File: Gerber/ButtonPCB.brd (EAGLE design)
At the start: 42 x 22 mm, 7 parts, among them SW1 SPST_TACT-EVQQ2, SW2 SPST_TACT-EVQQ2, SW3 SPST_TACT-EVQQ2

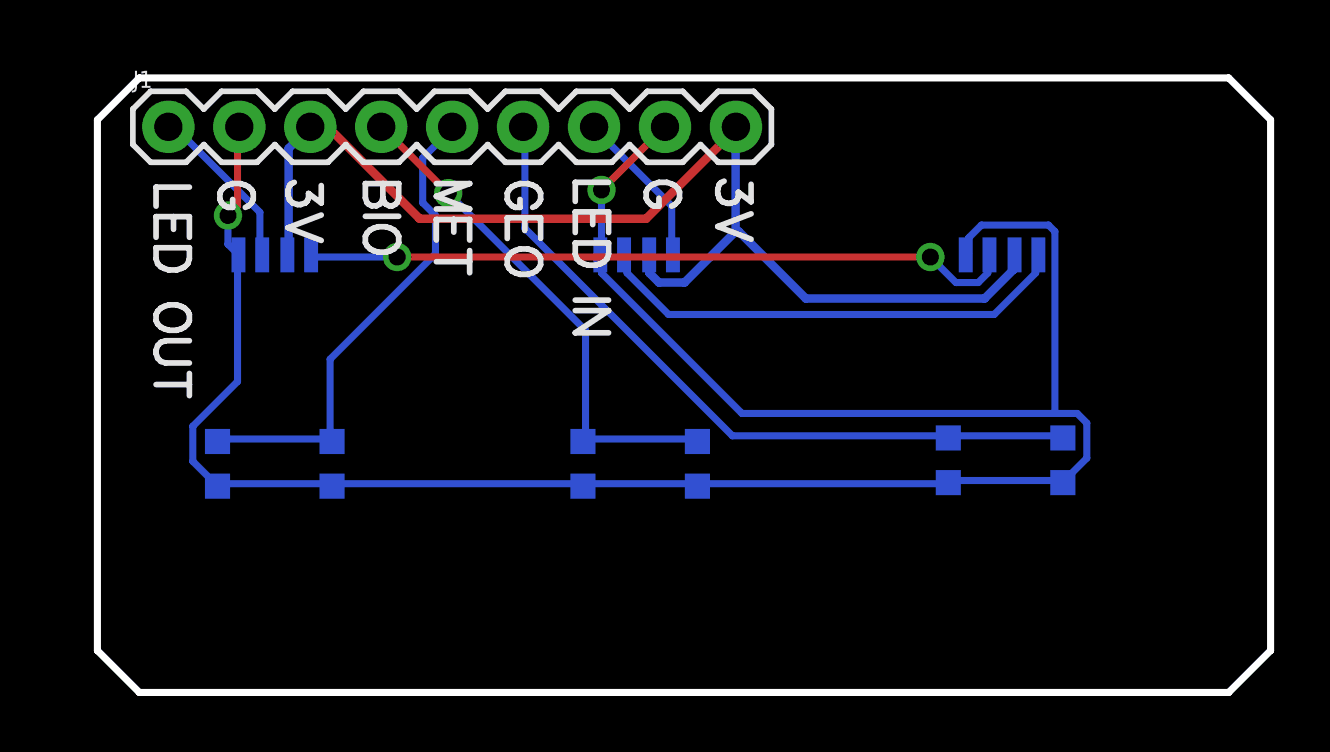
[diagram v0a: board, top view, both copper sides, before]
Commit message: Swapped to smd buttons that I like.
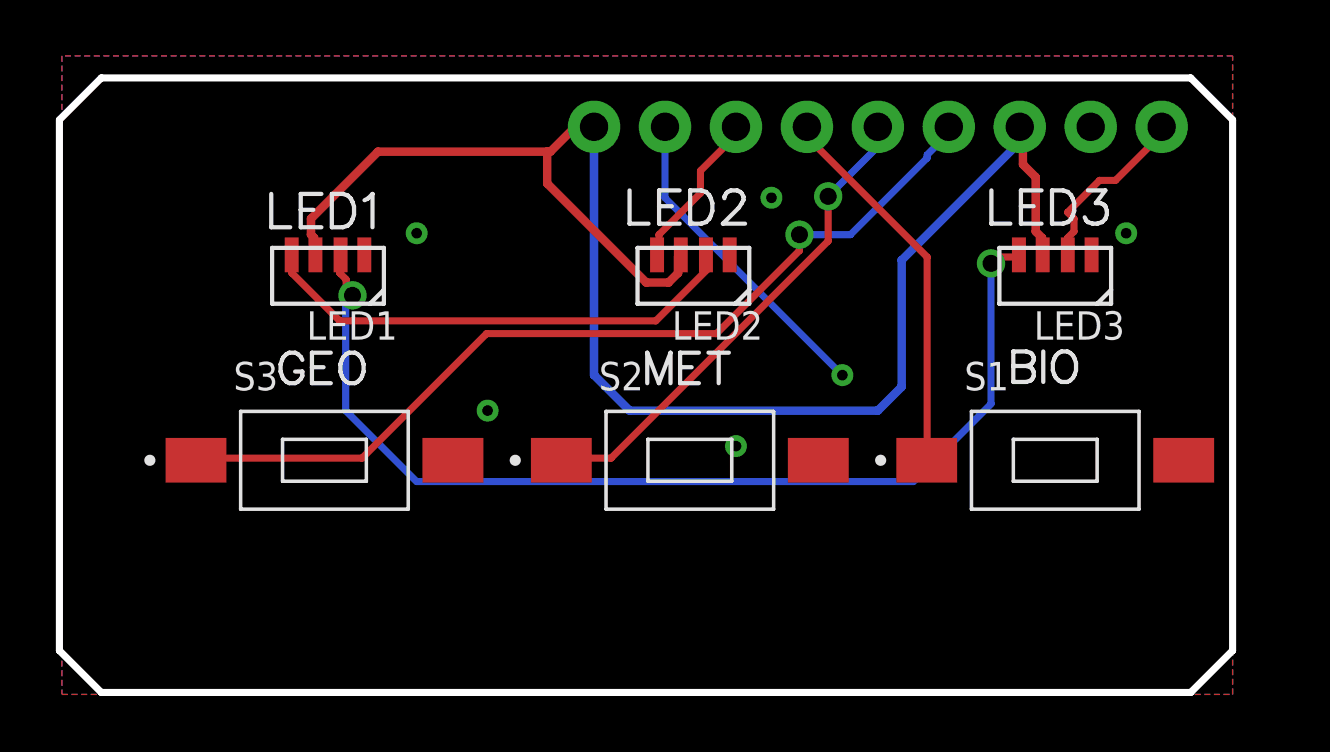
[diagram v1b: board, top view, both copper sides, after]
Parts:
- removed SW1, SW2, SW3: SPST_TACT-EVQQ2, microbuilder:BTN_KMR2_4.6X2.8
- added S1, S2, S3: 1437566-4, FSMSMTR-1437566-4:SW_1437566-4
- moved J1 35.6 mm to (39.4, 20.3), flipped to the bottom
- moved LED3 27.9 mm to (35.6, 15.0), flipped to the top
- moved LED1 24.1 mm to (9.53, 15.0), flipped to the top
- moved LED2 2.03 mm to (22.6, 15.0), flipped to the top
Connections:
- net BIO: now also S3.1; no longer SW3.A, SW3.A'
- net GEO: now also S1.1; no longer SW1.A, SW1.A'
- net GND: now also S1.2, S2.2, S3.2; no longer SW1.B, SW1.B', SW2.B, SW2.B', SW3.B, SW3.B'
- net MET: now also S2.1; no longer SW2.A, SW2.A'
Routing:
- net GND: track 83.8 -> 11.5 mm, vias 2 -> 6
- net V+: track 43.3 -> 57.9 mm
- net BIO: track 18.6 -> 32.5 mm
- net GEO: track 26.1 -> 13.7 mm
- net N$7: track 25.4 -> 37.3 mm
- net MET: track 17.7 -> 17.6 mm, vias 0 -> 1
- added copper zone on layer 1, net GND
- added copper zone on layer 16, net GND

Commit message: Added screw hole mounts to button pcb
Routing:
- net V+: track 57.9 -> 77.0 mm
- net N$6: track 17.5 -> 19.7 mm
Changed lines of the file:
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@@
 <setting verticaltext="up"/>
 </settings>
-<grid distance="0.05" unitdist="inch" unit="inch" style="lines" multiple="1" display="yes" altdistance="0.005" altunitdist="inch" altunit="inch"/>
+<grid distance="1" unitdist="mm" unit="mm" style="lines" multiple="1" display="yes" altdistance="0.1" altunitdist="mm" altunit="mm"/>
 <layers>
 <layer number="1" name="Top" color="4" fill="1" visible="yes" active="yes"/>
@@
 <layer number="44" name="Drills" color="7" fill="1" visible="no" active="yes"/>
 <layer number="45" name="Holes" color="7" fill="1" visible="yes" active="yes"/>
-<layer number="46" name="Milling" color="3" fill="1" visible="yes" active="yes"/>
+<layer number="46" name="Milling" color="3" fill="1" visible="no" active="yes"/>
 <layer number="47" name="Measures" color="7" fill="1" visible="no" active="yes"/>
 <layer number="48" name="Document" color="7" fill="1" visible="no" active="yes"/>
@@
 <wire x1="31.18045" y1="16.06071875" x2="31.12363125" y2="16.174359375" width="0.203" layer="22"/>
 <wire x1="31.12363125" y1="16.174359375" x2="31.12363125" y2="16.401640625" width="0.203" layer="22"/>
+<hole x="16.0655" y="14" drill="3.75"/>
+<hole x="29.083" y="14" drill="3.75"/>
 </plain>
 <attributes>
@@
 <wire x1="9.0297" y1="16.3449" x2="9.0297" y2="15.7734" width="0.3048" layer="1"/>
 <wire x1="8.9154" y1="16.4592" x2="9.0297" y2="16.3449" width="0.3048" layer="1"/>
-<wire x1="8.9154" y1="17.0307" x2="8.9154" y2="16.4592" width="0.3048" layer="1"/>
+<wire x1="8.9154" y1="17.0307" x2="8.9154" y2="16.8021" width="0.3048" layer="1"/>
+<wire x1="8.9154" y1="16.8021" x2="8.9154" y2="16.4592" width="0.3048" layer="1"/>
 <wire x1="11.3157" y1="19.431" x2="8.9154" y2="17.0307" width="0.3048" layer="1"/>
 <wire x1="17.4879" y1="19.431" x2="17.3736" y2="19.431" width="0.3048" layer="1"/>
@@
 <wire x1="17.3736" y1="19.431" x2="17.3736" y2="18.288" width="0.3048" layer="1"/>
 <wire x1="22.0599" y1="15.6591" x2="22.156" y2="15.736" width="0.3048" layer="1"/>
-<wire x1="34.29" y1="19.7739" x2="34.29" y2="20.32" width="0.3048" layer="16"/>
-<wire x1="30.0609" y1="15.5448" x2="34.29" y2="19.7739" width="0.3048" layer="16"/>
 <wire x1="19.0881" y1="20.2311" x2="19.05" y2="20.32" width="0.3048" layer="16"/>
-<wire x1="30.0609" y1="15.5448" x2="30.0609" y2="11.0109" width="0.3048" layer="16"/>
-<wire x1="30.0609" y1="11.0109" x2="29.21" y2="10.16" width="0.3048" layer="16"/>
-<wire x1="29.21" y1="10.16" x2="20.32" y2="10.16" width="0.3048" layer="16"/>
-<wire x1="20.32" y1="10.16" x2="19.05" y2="11.43" width="0.3048" layer="16"/>
-<wire x1="19.05" y1="11.43" x2="19.05" y2="20.32" width="0.3048" layer="16"/>
+<wire x1="35.0901" y1="10.0584" x2="35.0901" y2="15.6591" width="0.3048" layer="1"/>
+<wire x1="32.2326" y1="7.2009" x2="35.0901" y2="10.0584" width="0.3048" layer="1"/>
+<wire x1="3.5433" y1="7.2009" x2="32.2326" y2="7.2009" width="0.3048" layer="1"/>
+<wire x1="3.3147" y1="7.4295" x2="3.5433" y2="7.2009" width="0.3048" layer="1"/>
+<wire x1="3.3147" y1="12.2301" x2="3.3147" y2="7.4295" width="0.3048" layer="1"/>
+<wire x1="7.8867" y1="16.8021" x2="3.3147" y2="12.2301" width="0.3048" layer="1"/>
+<wire x1="8.9154" y1="16.8021" x2="7.8867" y2="16.8021" width="0.3048" layer="1"/>
+<wire x1="35.0901" y1="15.6591" x2="35.11" y2="15.736" width="0.3048" layer="1"/>
 </signal>
 <signal name="LED_IN">
@@
 <contactref element="LED1" pad="1"/>
 <contactref element="LED2" pad="3"/>
-<wire x1="8.2296" y1="15.0876" x2="8.2296" y2="15.6591" width="0.254" layer="1"/>
-<wire x1="9.9441" y1="13.3731" x2="8.2296" y2="15.0876" width="0.254" layer="1"/>
-<wire x1="21.2598" y1="13.3731" x2="9.9441" y2="13.3731" width="0.254" layer="1"/>
-<wire x1="23.0886" y1="15.2019" x2="21.2598" y2="13.3731" width="0.254" layer="1"/>
-<wire x1="23.0886" y1="15.6591" x2="23.0886" y2="15.2019" width="0.254" layer="1"/>
+<wire x1="8.2296" y1="15.2019" x2="8.2296" y2="15.6591" width="0.254" layer="1"/>
+<wire x1="10.0584" y1="13.3731" x2="8.2296" y2="15.2019" width="0.254" layer="1"/>
+<wire x1="11.0871" y1="13.3731" x2="10.0584" y2="13.3731" width="0.254" layer="1"/>
+<wire x1="14.7447" y1="17.0307" x2="11.0871" y2="13.3731" width="0.254" layer="1"/>
+<wire x1="17.9451" y1="17.0307" x2="14.7447" y2="17.0307" width="0.254" layer="1"/>
+<wire x1="20.8026" y1="14.1732" x2="17.9451" y2="17.0307" width="0.254" layer="1"/>
+<wire x1="21.9456" y1="14.1732" x2="20.8026" y2="14.1732" width="0.254" layer="1"/>
+<wire x1="22.9743" y1="15.2019" x2="21.9456" y2="14.1732" width="0.254" layer="1"/>
+<wire x1="22.9743" y1="15.6591" x2="22.9743" y2="15.2019" width="0.254" layer="1"/>
 <wire x1="8.2296" y1="15.6591" x2="8.225" y2="15.736" width="0.254" layer="1"/>
-<wire x1="23.0886" y1="15.6591" x2="23.056" y2="15.736" width="0.254" layer="1"/>
+<wire x1="22.9743" y1="15.6591" x2="23.056" y2="15.736" width="0.254" layer="1"/>
 </signal>
 <signal name="N$7">
@@
 <contactref element="J1" pad="4"/>
 <contactref element="S3" pad="1"/>
-<wire x1="10.7442" y1="8.4582" x2="4.8006" y2="8.4582" width="0.254" layer="1"/>
-<wire x1="15.2019" y1="12.9159" x2="10.7442" y2="8.4582" width="0.254" layer="1"/>
-<wire x1="23.4315" y1="12.9159" x2="15.2019" y2="12.9159" width="0.254" layer="1"/>
-<wire x1="26.4033" y1="15.8877" x2="23.4315" y2="12.9159" width="0.254" layer="1"/>
-<wire x1="26.4033" y1="16.4592" x2="26.4033" y2="15.8877" width="0.254" layer="1"/>
-<wire x1="28.2321" y1="16.4592" x2="26.4033" y2="16.4592" width="0.254" layer="16"/>
-<wire x1="30.9753" y1="19.2024" x2="28.2321" y2="16.4592" width="0.254" layer="16"/>
+<wire x1="11.6586" y1="8.4582" x2="4.8006" y2="8.4582" width="0.254" layer="1"/>
+<wire x1="14.1732" y1="10.9728" x2="11.6586" y2="8.4582" width="0.254" layer="1"/>
+<wire x1="20.574" y1="10.9728" x2="14.1732" y2="10.9728" width="0.254" layer="1"/>
+<wire x1="26.289" y1="16.6878" x2="20.574" y2="10.9728" width="0.254" layer="1"/>
+<wire x1="26.4033" y1="16.6878" x2="26.289" y2="16.6878" width="0.254" layer="16"/>
+<wire x1="26.6319" y1="16.4592" x2="26.4033" y2="16.6878" width="0.254" layer="16"/>
+<wire x1="27.2034" y1="16.4592" x2="26.6319" y2="16.4592" width="0.254" layer="16"/>
+<wire x1="27.6606" y1="16.9164" x2="27.2034" y2="16.4592" width="0.254" layer="16"/>
+<wire x1="27.7749" y1="16.9164" x2="27.6606" y2="16.9164" width="0.254" layer="16"/>
+<wire x1="28.575" y1="17.7165" x2="27.7749" y2="16.9164" width="0.254" layer="16"/>
+<wire x1="29.4894" y1="17.7165" x2="28.575" y2="17.7165" width="0.254" layer="16"/>
+<wire x1="30.9753" y1="19.2024" x2="29.4894" y2="17.7165" width="0.254" layer="16"/>
 <wire x1="30.9753" y1="19.3167" x2="30.9753" y2="19.2024" width="0.254" layer="16"/>
 <wire x1="31.6611" y1="20.0025" x2="30.9753" y2="19.3167" width="0.254" layer="16"/>
@@
 <wire x1="4.8006" y1="8.4582" x2="4.798" y2="8.382" width="0.254" layer="1"/>
 <wire x1="31.6611" y1="20.2311" x2="31.75" y2="20.32" width="0.254" layer="16"/>
-<via x="26.4033" y="16.4592" extent="1-16" drill="0.6096"/>
+<via x="26.289" y="16.6878" extent="1-16" drill="0.6096"/>
 </signal>
 </signals>

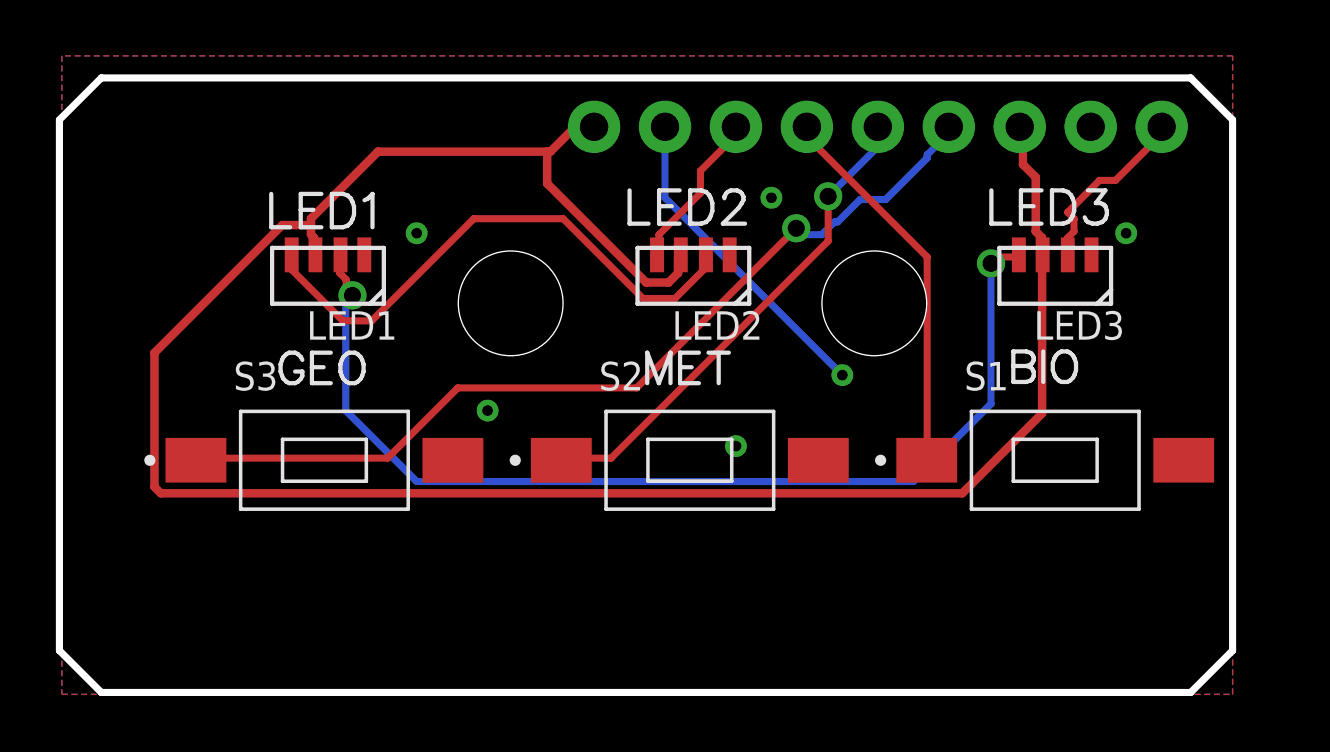
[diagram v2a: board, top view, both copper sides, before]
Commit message: Added lcd bezel
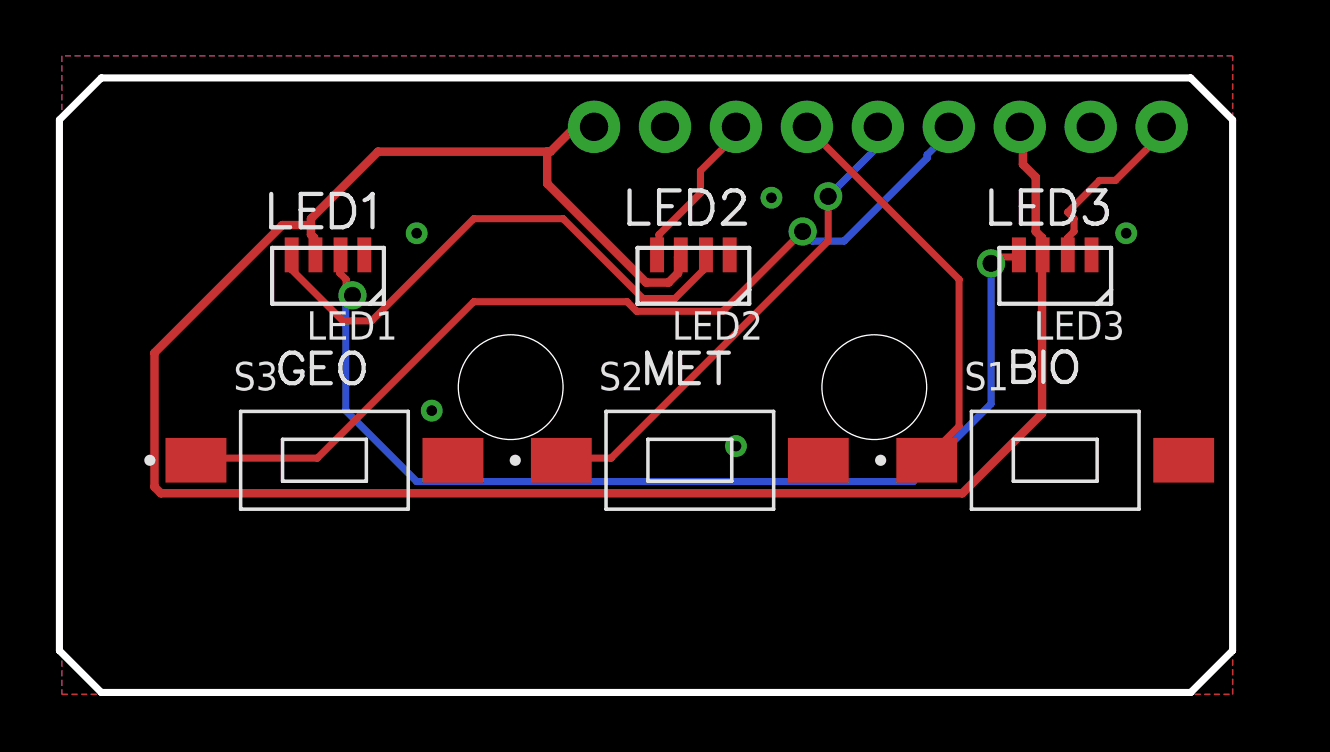
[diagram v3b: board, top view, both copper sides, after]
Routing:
- net GND: track 11.5 -> 0.00 mm, vias 6 -> 5
- net GEO: track 13.7 -> 14.7 mm
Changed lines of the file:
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@@
 <wire x1="31.18045" y1="16.06071875" x2="31.12363125" y2="16.174359375" width="0.203" layer="22"/>
 <wire x1="31.12363125" y1="16.174359375" x2="31.12363125" y2="16.401640625" width="0.203" layer="22"/>
-<hole x="16.0655" y="14" drill="3.75"/>
-<hole x="29.083" y="14" drill="3.75"/>
+<hole x="16.0655" y="11" drill="3.75"/>
+<hole x="29.083" y="11" drill="3.75"/>
 </plain>
 <attributes>
@@
 </polygon>
 <via x="12.7" y="16.51" extent="1-16" drill="0.381"/>
-<via x="27.94" y="11.43" extent="1-16" drill="0.381"/>
-<wire x1="21.59" y1="20.32" x2="21.59" y2="17.78" width="0.254" layer="16"/>
-<wire x1="21.59" y1="17.78" x2="27.94" y2="11.43" width="0.254" layer="16"/>
 <via x="38.1" y="16.51" extent="1-16" drill="0.381"/>
 <via x="25.4" y="17.78" extent="1-16" drill="0.381"/>
 <via x="24.13" y="8.89" extent="1-16" drill="0.381"/>
-<via x="15.24" y="10.16" extent="1-16" drill="0.381"/>
+<via x="13.24" y="10.16" extent="1-16" drill="0.381"/>
 </signal>
 <signal name="V+" class="1">
@@
 <contactref element="J1" pad="6"/>
 <contactref element="S1" pad="1"/>
-<wire x1="30.9753" y1="15.6591" x2="30.9753" y2="8.4582" width="0.254" layer="1"/>
-<wire x1="26.7462" y1="19.8882" x2="30.9753" y2="15.6591" width="0.254" layer="1"/>
-<wire x1="26.7462" y1="20.2311" x2="26.7462" y2="19.8882" width="0.254" layer="1"/>
+<wire x1="32.1183" y1="9.6012" x2="30.9753" y2="8.4582" width="0.254" layer="1"/>
+<wire x1="32.1183" y1="14.859" x2="32.1183" y2="9.6012" width="0.254" layer="1"/>
+<wire x1="26.7462" y1="20.2311" x2="32.1183" y2="14.859" width="0.254" layer="1"/>
 <wire x1="30.9753" y1="8.4582" x2="30.96" y2="8.382" width="0.254" layer="1"/>
 <wire x1="26.7462" y1="20.2311" x2="26.67" y2="20.32" width="0.254" layer="1"/>
@@
 <contactref element="J1" pad="4"/>
 <contactref element="S3" pad="1"/>
-<wire x1="11.6586" y1="8.4582" x2="4.8006" y2="8.4582" width="0.254" layer="1"/>
-<wire x1="14.1732" y1="10.9728" x2="11.6586" y2="8.4582" width="0.254" layer="1"/>
-<wire x1="20.574" y1="10.9728" x2="14.1732" y2="10.9728" width="0.254" layer="1"/>
-<wire x1="26.289" y1="16.6878" x2="20.574" y2="10.9728" width="0.254" layer="1"/>
-<wire x1="26.4033" y1="16.6878" x2="26.289" y2="16.6878" width="0.254" layer="16"/>
-<wire x1="26.6319" y1="16.4592" x2="26.4033" y2="16.6878" width="0.254" layer="16"/>
-<wire x1="27.2034" y1="16.4592" x2="26.6319" y2="16.4592" width="0.254" layer="16"/>
-<wire x1="27.6606" y1="16.9164" x2="27.2034" y2="16.4592" width="0.254" layer="16"/>
-<wire x1="27.7749" y1="16.9164" x2="27.6606" y2="16.9164" width="0.254" layer="16"/>
-<wire x1="28.575" y1="17.7165" x2="27.7749" y2="16.9164" width="0.254" layer="16"/>
-<wire x1="29.4894" y1="17.7165" x2="28.575" y2="17.7165" width="0.254" layer="16"/>
-<wire x1="30.9753" y1="19.2024" x2="29.4894" y2="17.7165" width="0.254" layer="16"/>
+<wire x1="9.144" y1="8.4582" x2="4.8006" y2="8.4582" width="0.254" layer="1"/>
+<wire x1="14.7447" y1="14.0589" x2="9.144" y2="8.4582" width="0.254" layer="1"/>
+<wire x1="20.2311" y1="14.0589" x2="14.7447" y2="14.0589" width="0.254" layer="1"/>
+<wire x1="20.574" y1="13.716" x2="20.2311" y2="14.0589" width="0.254" layer="1"/>
+<wire x1="23.6601" y1="13.716" x2="20.574" y2="13.716" width="0.254" layer="1"/>
+<wire x1="26.5176" y1="16.5735" x2="23.6601" y2="13.716" width="0.254" layer="1"/>
+<wire x1="26.8605" y1="16.2306" x2="26.5176" y2="16.5735" width="0.254" layer="16"/>
+<wire x1="28.0035" y1="16.2306" x2="26.8605" y2="16.2306" width="0.254" layer="16"/>
+<wire x1="30.9753" y1="19.2024" x2="28.0035" y2="16.2306" width="0.254" layer="16"/>
 <wire x1="30.9753" y1="19.3167" x2="30.9753" y2="19.2024" width="0.254" layer="16"/>
 <wire x1="31.6611" y1="20.0025" x2="30.9753" y2="19.3167" width="0.254" layer="16"/>
@@
 <wire x1="4.8006" y1="8.4582" x2="4.798" y2="8.382" width="0.254" layer="1"/>
 <wire x1="31.6611" y1="20.2311" x2="31.75" y2="20.32" width="0.254" layer="16"/>
-<via x="26.289" y="16.6878" extent="1-16" drill="0.6096"/>
+<via x="26.5176" y="16.5735" extent="1-16" drill="0.6096"/>
 </signal>
 </signals>

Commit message: minor updates, notes
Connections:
- net BIO renamed BIO_BUTTON
- net GEO renamed GEO_BUTTON
- net MET renamed MET_BUTTON
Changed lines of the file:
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@@
 <wire x1="39.3192" y1="20.2311" x2="39.37" y2="20.32" width="0.254" layer="1"/>
 </signal>
-<signal name="GEO">
+<signal name="GEO_BUTTON">
 <contactref element="J1" pad="6"/>
 <contactref element="S1" pad="1"/>
@@
 <wire x1="26.7462" y1="20.2311" x2="26.67" y2="20.32" width="0.254" layer="1"/>
 </signal>
-<signal name="MET">
+<signal name="MET_BUTTON">
 <contactref element="J1" pad="5"/>
 <contactref element="S2" pad="1"/>
@@
 <via x="27.432" y="17.8308" extent="1-16" drill="0.6096"/>
 </signal>
-<signal name="BIO">
+<signal name="BIO_BUTTON">
 <contactref element="J1" pad="4"/>
 <contactref element="S3" pad="1"/>
